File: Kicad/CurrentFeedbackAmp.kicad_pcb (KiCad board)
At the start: 2 copper layers, 200 x 100 mm, 123 parts, among them J1 Test_Etapa_3_Inf, J10 Protecc_Sup_In1, J11 Protecc_Inf_In1, J12 Protecc_Sup_In2, J13 Test_Etapa_3_Inf, J14 Entrada, J15 Salida masa2, J16 Salida tierra, J17 Salida senal, J2 Test_Realim_Out, J3 Salida masa1, J4 Protecc_Sup_Out, J5 Protecc_Inf_Out, J6 Conector Vcc, J7 Conector Vdd, J8 Test_Etapa_3_Inf, J9 Test_Etapa_3_Sup, Q1 TIP42C, Q10 BC858, Q11 BC848, Q12 BC858, Q13 BC559, Q14 BC559, Q15 BC559, Q16 BC549, Q17 BC549, Q18 BC549, Q19 BC559, Q2 BD135, Q20 BC549, Q21 BC559, Q22 BC549, Q23 BC848, Q24 BD136, Q25 BC858, Q26 BC848, Q27 BC848, Q28 BC848, Q29 BC858, Q3 BD136, Q30 BC858, Q31 BC848, Q32 BC858, Q33 BD135, Q34 TIP41C, Q35 BC858, Q36 BC848, Q37 BC848, Q38 BC848, Q4 BC848, Q40 BC858, Q41 BC858, Q5 BC848, Q6 BC858, Q7 BC858, Q8 BC848, Q9 BC858, U1 LM7812_TO220, U2 TL082, U3 LM7912_TO220, U4 LM7805_TO220, U5 LM7905_TO220

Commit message: Todos los componentes colocados en la placa, faltan hacer mejoras pero al menos demuestra que es posible terminarla :D
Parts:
- R19, R22, R24: moved to B.Cu
- R32: moved to F.Cu
- moved J16 195.9 mm to (117.5, 102.0)
- moved C6 184.0 mm to (86.5, 104.0), turned to 270 degrees
- moved R22 183.8 mm to (97.0, 104.0), turned to 0 degrees
- moved C12 175.2 mm to (82.0, 104.0), turned to 270 degrees
- moved J13 174.2 mm to (12.0, 76.5)
- moved J2 168.9 mm to (74.0, 92.0)
- moved R23 165.4 mm to (83.0, 99.0), turned to 180 degrees
- moved C11 159.4 mm to (83.5, 90.0)
- moved J17 159.2 mm to (73.0, 106.0)
- moved J15 155.4 mm to (103.6, 47.8)
- moved C5 149.8 mm to (83.5, 85.5)
- moved J3 149.2 mm to (88.6, 47.8)
- moved U2 148.7 mm to (93.4, 91.0), turned to 0 degrees
- moved R24 147.0 mm to (93.0, 83.0), turned to 90 degrees
- moved R19 145.0 mm to (78.0, 93.0), turned to 90 degrees
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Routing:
- net GND: track 0.13 -> 342.2 mm, vias 0 -> 4
- net Vout: track 63.6 -> 177.8 mm, vias 0 -> 1
- net VccTL: track 0.00 -> 91.3 mm
- net VddTL: track 0.00 -> 79.2 mm, vias 0 -> 1
- net Vin-: track 69.8 -> 123.8 mm, vias 0 -> 1
- net Vdd: track 123.4 -> 171.0 mm, vias 0 -> 2
- net Net-(C11-Pad1): track 0.00 -> 32.7 mm
- net Net-(C12-Pad1): track 0.00 -> 28.7 mm, vias 0 -> 1
- net Vcc: track 158.7 -> 186.7 mm
- net Vdd5: track 43.8 -> 59.7 mm
- net Net-(C11-Pad2): track 0.00 -> 15.4 mm
- net Net-(Q36-Pad3): track 0.00 -> 13.2 mm
- net Net-(R32-Pad1): track 4.64 -> 16.7 mm, vias 0 -> 1
- net Net-(J13-Pad1): track 66.1 -> 72.4 mm
- net Net-(J10-Pad1): track 78.6 -> 84.9 mm
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
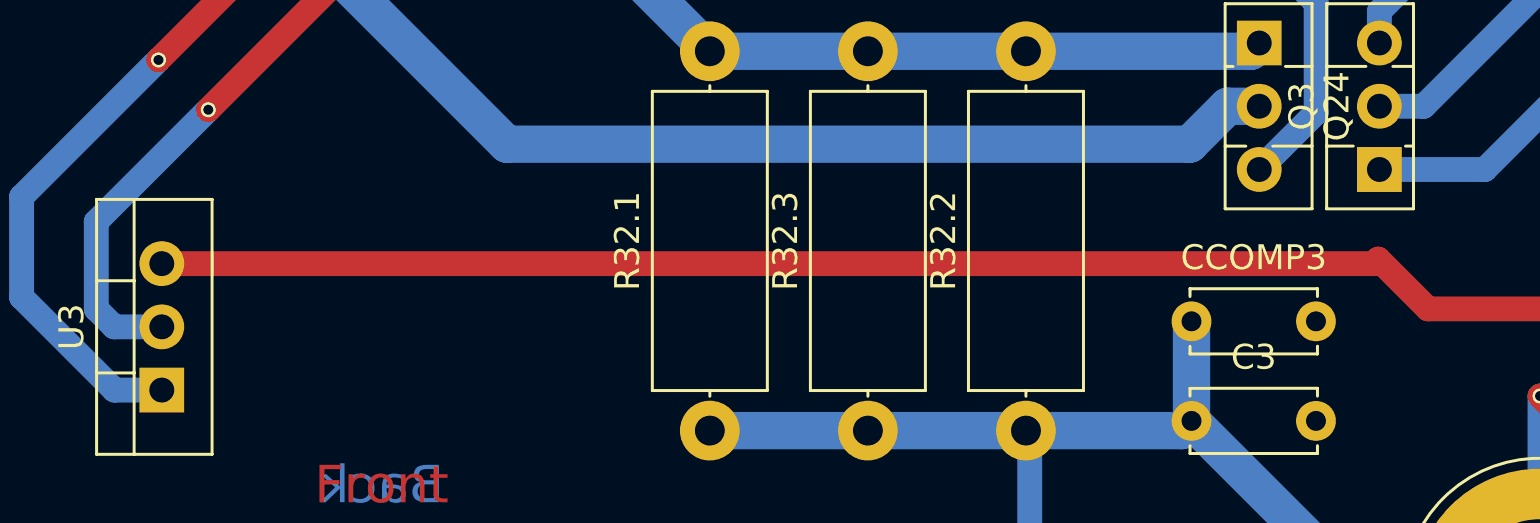
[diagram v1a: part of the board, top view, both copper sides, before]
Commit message: Arreglo una conexion a los TL que estaba en la capa frontal pero tenia que ir en la trasera (ese truquito solo sirve para capacitores y resistencias tht)
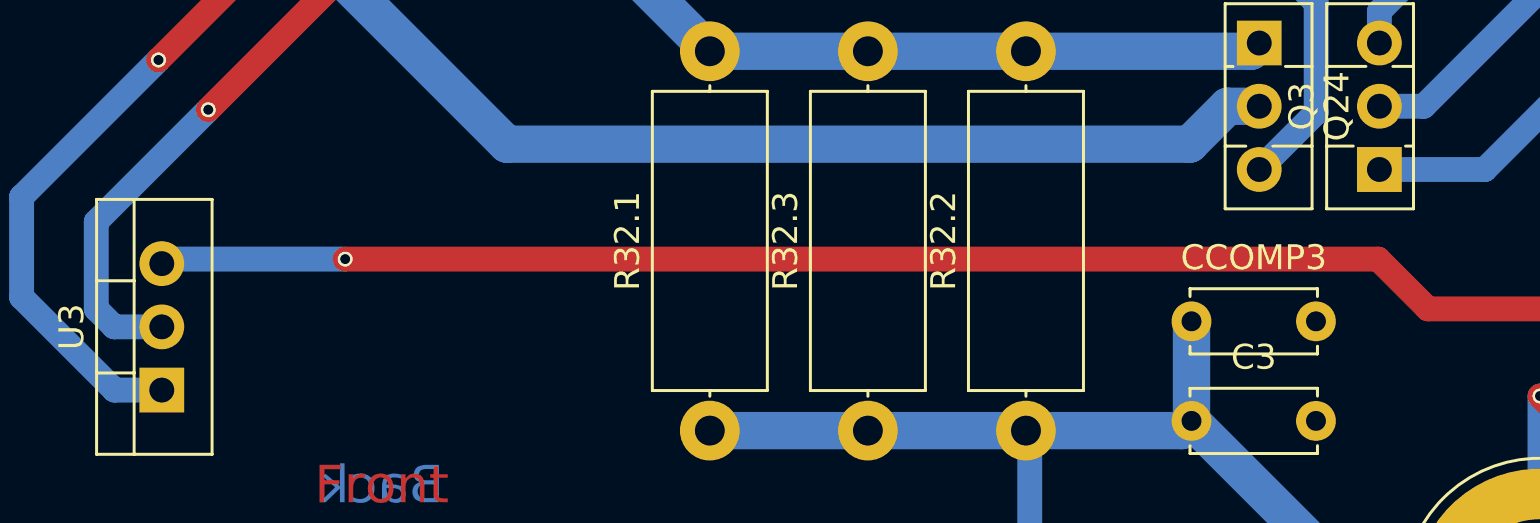
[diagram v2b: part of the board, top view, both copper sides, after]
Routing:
- net VddTL: vias 1 -> 2
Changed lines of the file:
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@@
   (general
     (links 203)
-    (no_connects 63)
-    (area 3.036599 12.797799 203.186601 112.947801)
+    (no_connects 20)
+    (area 1.164338 -6.909481 204.715363 113.4188)
     (thickness 1.6)
     (drawings 6)
-    (tracks 668)
+    (tracks 670)
     (zones 0)
     (modules 123)
@@
   (segment (start 101 91) (end 103.2 91) (width 1) (layer F.Cu) (net 35))
   (segment (start 103.2 91) (end 104.2 92) (width 1) (layer F.Cu) (net 35))
-  (segment (start 66.5 92.5) (end 66.31794 92.68206) (width 1) (layer F.Cu) (net 36))
-  (segment (start 66.31794 92.68206) (end 17.63268 92.68206) (width 1) (layer F.Cu) (net 36))
+  (segment (start 25 92.5) (end 17.81474 92.5) (width 1) (layer B.Cu) (net 36))
+  (segment (start 17.81474 92.5) (end 17.63268 92.68206) (width 1) (layer B.Cu) (net 36))
+  (via (at 25 92.5) (size 0.6) (drill 0.4) (layers F.Cu B.Cu) (net 36))
+  (segment (start 66.5 92.5) (end 25 92.5) (width 1) (layer F.Cu) (net 36))
   (segment (start 68.5 94.5) (end 66.5 92.5) (width 1) (layer F.Cu) (net 36))
   (segment (start 86.5 94.5) (end 68.5 94.5) (width 1) (layer F.Cu) (net 36))

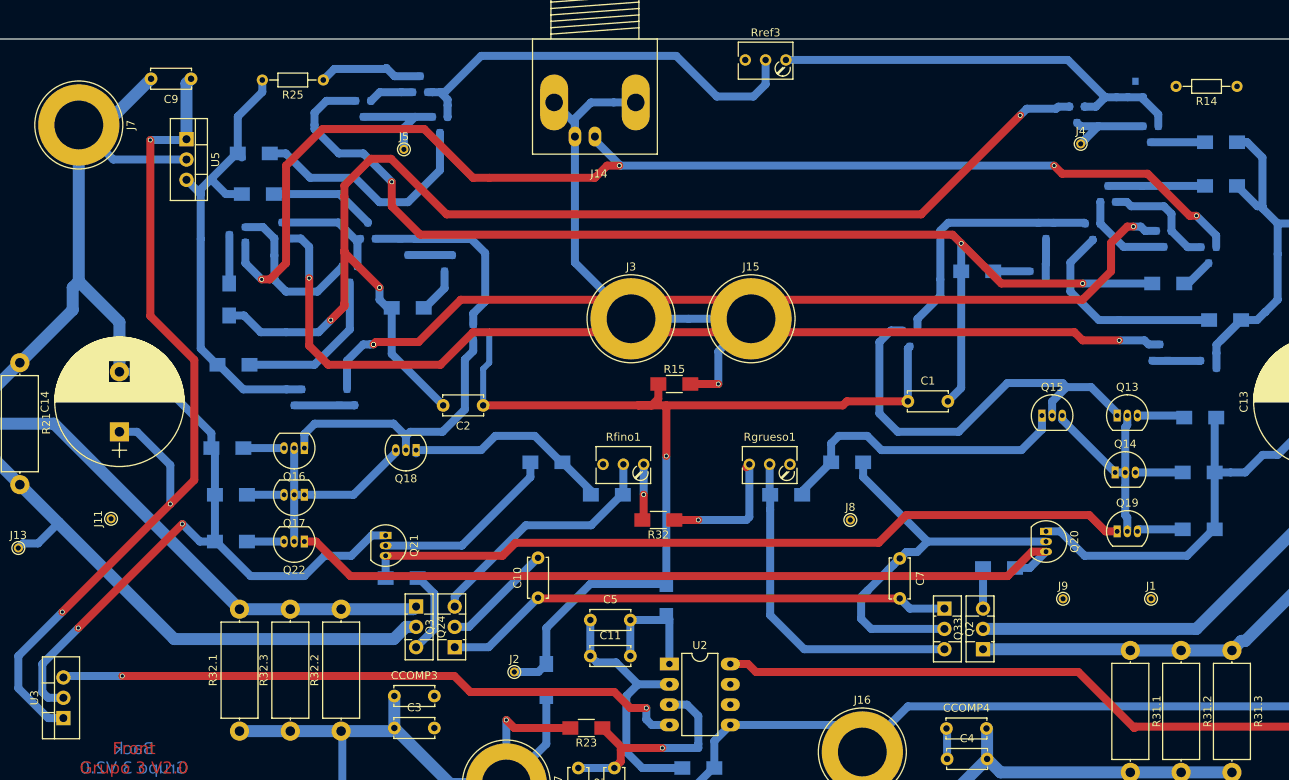
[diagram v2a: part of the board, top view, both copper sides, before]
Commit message: Algunas conexiones mas, incluida la de retorno de masa que va por el "medio" de la placa
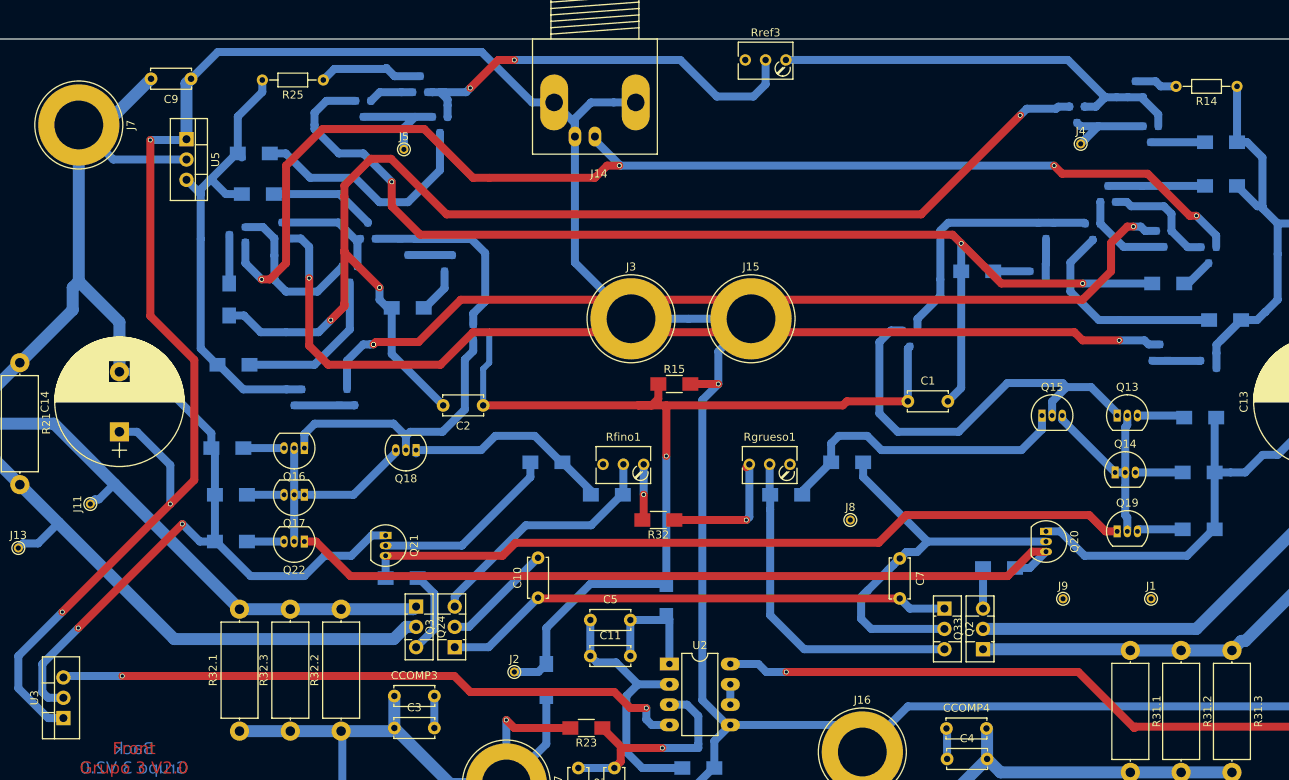
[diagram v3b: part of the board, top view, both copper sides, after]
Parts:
- moved J11 3.18 mm to (21.0, 71.0)
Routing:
- net GND: track 342.2 -> 436.7 mm
- net Vcc5: track 48.4 -> 55.3 mm
- net Net-(Q41-Pad3): track 0.00 -> 5.34 mm
- net Net-(J11-Pad1): track 65.1 -> 69.1 mm
- net Net-(C3-Pad2): track 35.3 -> 39.3 mm
- net Net-(U2-Pad6): track 0.00 -> 2.54 mm
- net Net-(Q36-Pad1): track 59.1 -> 59.2 mm, vias 0 -> 2
- net VccTL: vias 0 -> 1
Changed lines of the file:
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@@
     (thickness 1.6)
     (drawings 6)
-    (tracks 670)
+    (tracks 694)
     (zones 0)
     (modules 123)
@@
   )
   (module Connectors:PINTST (layer F.Cu)
-    (at 23.59 72.846 90)
+    (at 21 71 90)
     (descr "module 1 pin (ou trou mecanique de percage)")
     (tags DEV)
@@
     (effects (font (size 1.5 1.5) (thickness 0.3)) (justify mirror))
   )
+  (segment (start 64 95) (end 64 99) (width 1) (layer B.Cu) (net 1))
   (segment (start 65.024 61.976) (end 60.988 61.976) (width 1) (layer B.Cu) (net 1))
   (segment (start 60.988 61.976) (end 60.452 62.512) (width 1) (layer B.Cu) (net 1))
@@
   (segment (start 93.38 96.08) (end 95.58 96.08) (width 1) (layer B.Cu) (net 5))
   (segment (start 95.58 96.08) (end 97 97.5) (width 1) (layer B.Cu) (net 5))
+  (segment (start 69.92356 14.5) (end 36.936 14.5) (width 1) (layer B.Cu) (net 6))
+  (segment (start 36.936 14.5) (end 33.59 17.846) (width 1) (layer B.Cu) (net 6))
+  (segment (start 78.97622 20.8026) (end 76.22616 20.8026) (width 1) (layer B.Cu) (net 6))
+  (segment (start 76.22616 20.8026) (end 69.92356 14.5) (width 1) (layer B.Cu) (net 6))
+  (segment (start 101 98.62) (end 100.6 98.62) (width 1) (layer B.Cu) (net 6))
+  (segment (start 100.6 98.62) (end 97.5 95.52) (width 1) (layer B.Cu) (net 6))
+  (segment (start 97.5 95.52) (end 97.5 58) (width 1) (layer B.Cu) (net 6))
+  (segment (start 97.5 58) (end 99.5 56) (width 1) (layer B.Cu) (net 6))
   (segment (start 34 53) (end 28.5 47.5) (width 1) (layer F.Cu) (net 6))
   (segment (start 28.5 47.5) (end 28.5 25.5) (width 1) (layer F.Cu) (net 6))
@@
   (segment (start 132.588 89.154) (end 150.847982 89.154) (width 1.5) (layer B.Cu) (net 12))
   (segment (start 150.847982 89.154) (end 151.001026 89.307044) (width 1.5) (layer B.Cu) (net 12))
-  (segment (start 39.6494 84.1502) (end 16.4592 60.96) (width 1.5) (layer B.Cu) (net 13))
+  (segment (start 39.6494 84.1502) (end 24 68.5008) (width 1.5) (layer B.Cu) (net 13))
+  (segment (start 24 68.5008) (end 16.4592 60.96) (width 1.5) (layer B.Cu) (net 13))
+  (segment (start 21 71) (end 21.571499 70.428501) (width 1) (layer B.Cu) (net 13))
+  (segment (start 21.571499 70.428501) (end 22.072299 70.428501) (width 1) (layer B.Cu) (net 13))
+  (segment (start 22.072299 70.428501) (end 24 68.5008) (width 1) (layer B.Cu) (net 13))
   (segment (start 16.4592 60.96) (end 6.35 60.96) (width 1.5) (layer B.Cu) (net 13))
   (segment (start 52.3494 84.1502) (end 61.3918 84.1502) (width 1.5) (layer B.Cu) (net 13))
@@
   (segment (start 149.288 20.161) (end 150.688 20.161) (width 1) (layer B.Cu) (net 26))
   (segment (start 145.283 21.336) (end 145.283 21.286) (width 1) (layer B.Cu) (net 26))
+  (segment (start 94.748 15.5) (end 99.314 20.066) (width 1) (layer B.Cu) (net 27))
+  (segment (start 74 15.5) (end 94.748 15.5) (width 1) (layer B.Cu) (net 27))
+  (segment (start 72 15.5) (end 74 15.5) (width 1) (layer F.Cu) (net 27))
+  (via (at 74 15.5) (size 0.6) (drill 0.4) (layers F.Cu B.Cu) (net 27))
+  (segment (start 68.5 19) (end 72 15.5) (width 1) (layer F.Cu) (net 27))
+  (segment (start 67.974 19.526) (end 68.5 19) (width 1) (layer B.Cu) (net 27))
+  (via (at 68.5 19) (size 0.6) (drill 0.4) (layers F.Cu B.Cu) (net 27))
+  (segment (start 64.738 19.526) (end 67.974 19.526) (width 1) (layer B.Cu) (net 27))
   (segment (start 99.314 20.066) (end 103.886 20.066) (width 1) (layer B.Cu) (net 27))
   (segment (start 103.886 20.066) (end 105.41 18.542) (width 1) (layer B.Cu) (net 27))
-  (segment (start 94.234 14.986) (end 99.314 20.066) (width 1) (layer B.Cu) (net 27))
-  (segment (start 69.85 14.986) (end 94.234 14.986) (width 1) (layer B.Cu) (net 27))
-  (segment (start 65.31 19.526) (end 69.85 14.986) (width 1) (layer B.Cu) (net 27))
   (segment (start 64.738 19.526) (end 65.31 19.526) (width 1) (layer B.Cu) (net 27))
   (segment (start 105.41 15.494) (end 105.41 18.542) (width 1) (layer B.Cu) (net 27))
@@
   (segment (start 64.704 24.606) (end 64.704 24.704) (width 1) (layer B.Cu) (net 29))
   (segment (start 153.543 25.781) (end 160.338 25.781) (width 1) (layer B.Cu) (net 30))
+  (segment (start 154.796 18.796) (end 154.161 18.161) (width 1) (layer B.Cu) (net 31))
+  (segment (start 154.161 18.161) (end 151.638 18.161) (width 1) (layer B.Cu) (net 31))
+  (segment (start 156.718 18.796) (end 154.796 18.796) (width 1) (layer B.Cu) (net 31))
+  (segment (start 101 96.08) (end 101 93.54) (width 1) (layer B.Cu) (net 32))
   (segment (start 193.59 77.846) (end 194.389999 77.046001) (width 1) (layer B.Cu) (net 33))
   (segment (start 194.389999 77.046001) (end 194.389999 70.945999) (width 1) (layer B.Cu) (net 33))
@@
   (segment (start 33.02 27.94) (end 23.876 27.94) (width 1) (layer B.Cu) (net 34))
   (segment (start 23.876 27.94) (end 19.558 23.622) (width 1) (layer B.Cu) (net 34))
+  (segment (start 105.5 92) (end 104.5 91) (width 1) (layer B.Cu) (net 35))
+  (segment (start 104.5 91) (end 101 91) (width 1) (layer B.Cu) (net 35))
+  (segment (start 108 92) (end 105.5 92) (width 1) (layer B.Cu) (net 35))
+  (via (at 108 92) (size 0.6) (drill 0.4) (layers F.Cu B.Cu) (net 35))
+  (segment (start 144.5 92) (end 108 92) (width 1) (layer F.Cu) (net 35))
   (segment (start 151.5 99) (end 151.66352 98.83648) (width 1) (layer F.Cu) (net 35))
   (segment (start 151.66352 98.83648) (end 188.93536 98.83648) (width 1) (layer F.Cu) (net 35))
   (segment (start 144.5 92) (end 151.5 99) (width 1) (layer F.Cu) (net 35))
-  (segment (start 104.2 92) (end 144.5 92) (width 1) (layer F.Cu) (net 35))
-  (segment (start 101 91) (end 103.2 91) (width 1) (layer F.Cu) (net 35))
-  (segment (start 103.2 91) (end 104.2 92) (width 1) (layer F.Cu) (net 35))
   (segment (start 25 92.5) (end 17.81474 92.5) (width 1) (layer B.Cu) (net 36))
   (segment (start 17.81474 92.5) (end 17.63268 92.68206) (width 1) (layer B.Cu) (net 36))
@@
   (segment (start 87.63 65.786) (end 87.63 69.786) (width 1) (layer B.Cu) (net 47))
   (segment (start 87.63 69.786) (end 87.566 69.85) (width 1) (layer B.Cu) (net 47))
+  (segment (start 164.338 25.781) (end 164.338 18.796) (width 1) (layer B.Cu) (net 48))
   (segment (start 161.766 54.036) (end 161.766 52.136) (width 1) (layer B.Cu) (net 48))
   (segment (start 161.766 52.136) (end 161.766 51.086) (width 1) (layer B.Cu) (net 48))
@@
   (segment (start 62.674 46.482) (end 62.824 46.482) (width 1) (layer B.Cu) (net 69))
   (segment (start 62.824 46.482) (end 65.278 44.028) (width 1) (layer B.Cu) (net 69))
+  (via (at 103 73) (size 0.6) (drill 0.4) (layers F.Cu B.Cu) (net 70))
+  (segment (start 96 73) (end 103 73) (width 1) (layer F.Cu) (net 70))
   (segment (start 103 73) (end 103.378 72.622) (width 1) (layer B.Cu) (net 70))
   (segment (start 103.378 72.622) (end 103.378 66.04) (width 1) (layer B.Cu) (net 70))
-  (segment (start 97 73) (end 103 73) (width 1) (layer B.Cu) (net 70))
-  (segment (start 96 73) (end 97 73) (width 1) (layer F.Cu) (net 70))
-  (via (at 97 73) (size 0.6) (drill 0.4) (layers F.Cu B.Cu) (net 70))
   (segment (start 94 73) (end 96 73) (width 1) (layer F.Cu) (net 70))
   (segment (start 103 66.418) (end 103.378 66.04) (width 1) (layer F.Cu) (net 70))
